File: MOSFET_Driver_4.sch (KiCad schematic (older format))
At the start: 20 parts, among them U1 FD6288Q

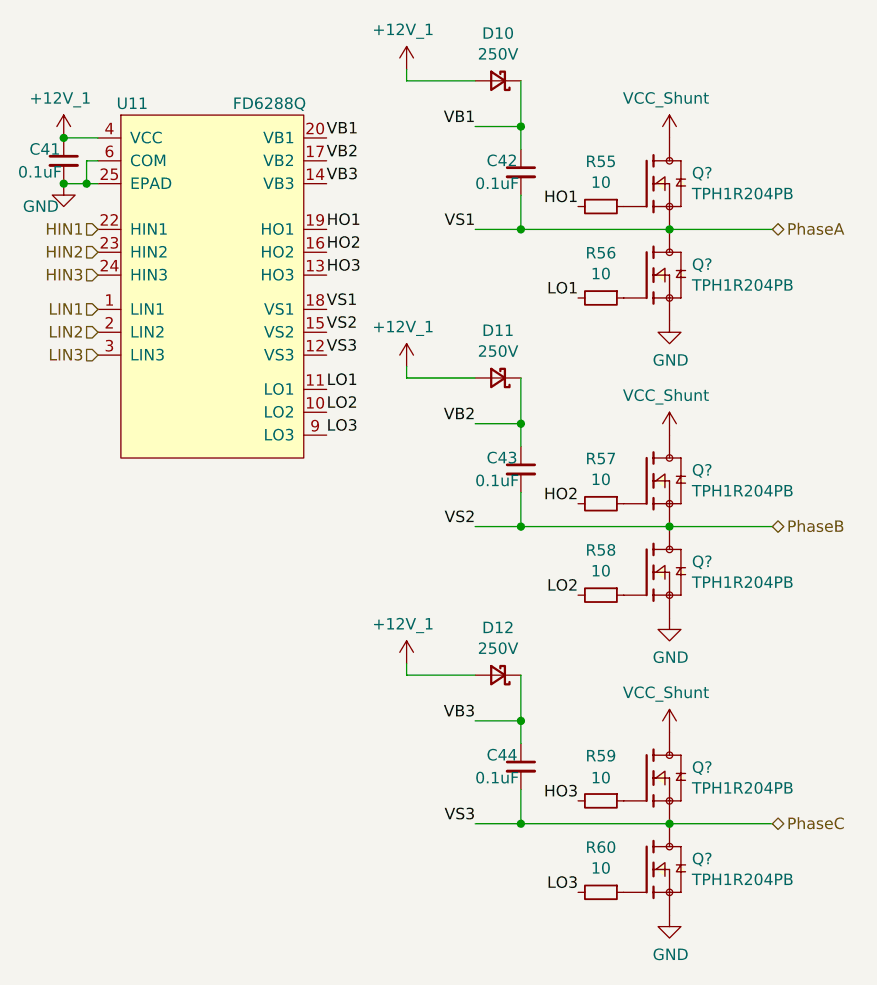
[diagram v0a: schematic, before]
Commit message: Started adding filtering caps
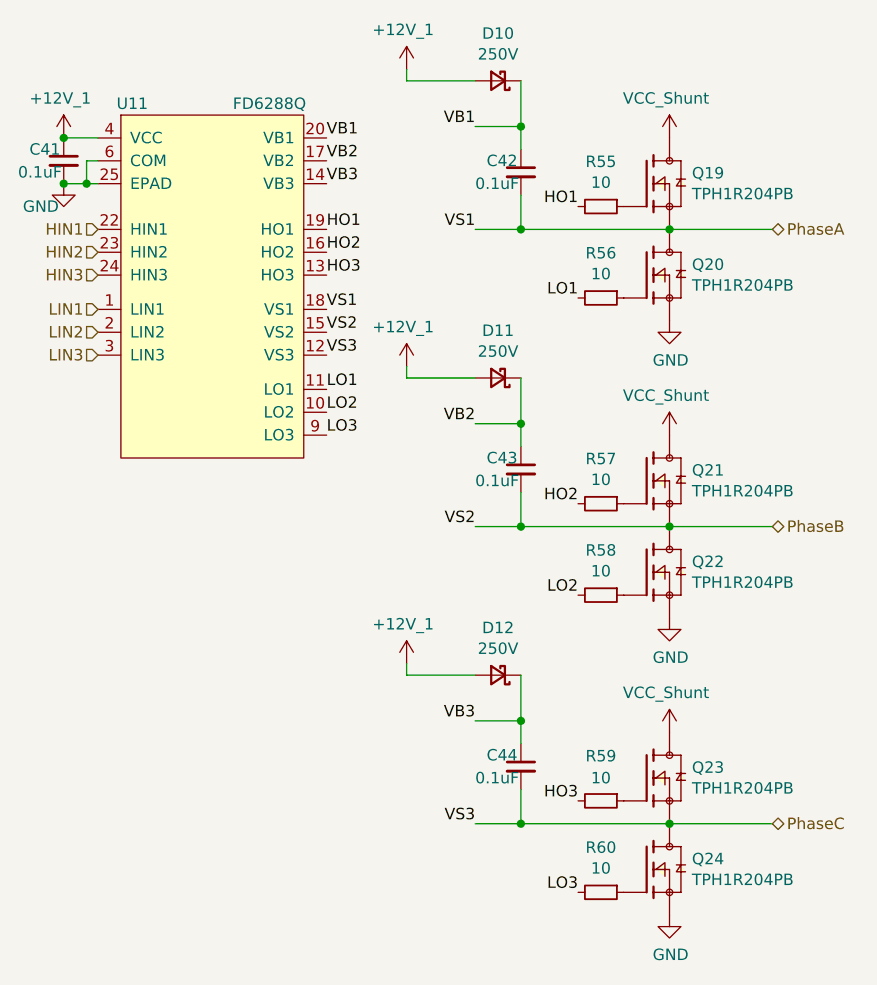
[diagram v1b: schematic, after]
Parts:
- gave numbers to parts that had none: 6
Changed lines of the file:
@@
 	7500 5000 8150 5000
 $Comp
-L JPW_Symbols:TPH1R204PB Q?
+L JPW_Symbols:TPH1R204PB Q19
 U 1 1 60824277
 P 8150 2200
-F 0 "Q?" H 8248 2246 50  0000 L CNN
+F 0 "Q19" H 8248 2246 50  0000 L CNN
 F 1 "TPH1R204PB" H 8248 2155 50  0000 L CNN
 F 2 "Footprints:TPH1R204PB" H 7900 2450 50  0001 L BNN
@@
 	8150 2400 8600 2400
 $Comp
-L JPW_Symbols:TPH1R204PB Q?
+L JPW_Symbols:TPH1R204PB Q20
 U 1 1 60825571
 P 8150 2600
-F 0 "Q?" H 8248 2646 50  0000 L CNN
+F 0 "Q20" H 8248 2646 50  0000 L CNN
 F 1 "TPH1R204PB" H 8248 2555 50  0000 L CNN
 F 2 "Footprints:TPH1R204PB" H 7900 2850 50  0001 L BNN
@@
 $EndComp
 $Comp
-L JPW_Symbols:TPH1R204PB Q?
+L JPW_Symbols:TPH1R204PB Q21
 U 1 1 6082647E
 P 8150 3500
-F 0 "Q?" H 8248 3546 50  0000 L CNN
+F 0 "Q21" H 8248 3546 50  0000 L CNN
 F 1 "TPH1R204PB" H 8248 3455 50  0000 L CNN
 F 2 "Footprints:TPH1R204PB" H 7900 3750 50  0001 L BNN
@@
 	8150 3700 8600 3700
 $Comp
-L JPW_Symbols:TPH1R204PB Q?
+L JPW_Symbols:TPH1R204PB Q22
 U 1 1 608273DC
 P 8150 3900
-F 0 "Q?" H 8248 3946 50  0000 L CNN
+F 0 "Q22" H 8248 3946 50  0000 L CNN
 F 1 "TPH1R204PB" H 8248 3855 50  0000 L CNN
 F 2 "Footprints:TPH1R204PB" H 7900 4150 50  0001 L BNN
@@
 $EndComp
 $Comp
-L JPW_Symbols:TPH1R204PB Q?
+L JPW_Symbols:TPH1R204PB Q23
 U 1 1 60828460
 P 8150 4800
-F 0 "Q?" H 8248 4846 50  0000 L CNN
+F 0 "Q23" H 8248 4846 50  0000 L CNN
 F 1 "TPH1R204PB" H 8248 4755 50  0000 L CNN
 F 2 "Footprints:TPH1R204PB" H 7900 5050 50  0001 L BNN
@@
 	8150 5000 8600 5000
 $Comp
-L JPW_Symbols:TPH1R204PB Q?
+L JPW_Symbols:TPH1R204PB Q24
 U 1 1 608296F7
 P 8150 5200
-F 0 "Q?" H 8248 5246 50  0000 L CNN
+F 0 "Q24" H 8248 5246 50  0000 L CNN
 F 1 "TPH1R204PB" H 8248 5155 50  0000 L CNN
 F 2 "Footprints:TPH1R204PB" H 7900 5450 50  0001 L BNN
